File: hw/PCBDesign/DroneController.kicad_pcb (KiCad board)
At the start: 4 copper layers, 100 x 50 mm, 194 parts, among them J1 SerialDebug, J10 SW_B, J11 YTrim, J12 SW_C, J13 TTrim, J14 SW_D, J2 USB_B_Micro, J3 ExtBatt, J4 Conn_ARM_JTAG_SWD_10, J5 EncoderConn, J6 JoystickConn, J7 PTrim, J8 SW_A, J9 RTrim, Q1 MMBT3904, Q2 si2302, Q3 si2302, Q4 si2301, Q5 si2301, SW13 Key_User, SW15 Key_nRESET, SW17 Key_nBOOT, U1 74HC165, U11 74HC595, U13 STM32F446RETx, U14 RN4871, U2 74HC165, U3 74HC165, U4 AT25SF081, U5 AT24C256, U6 NRF24L01_Breakout, U7 BQ24074RGT, U8 AMS1117-3.3, Y1 8MHz Crystal

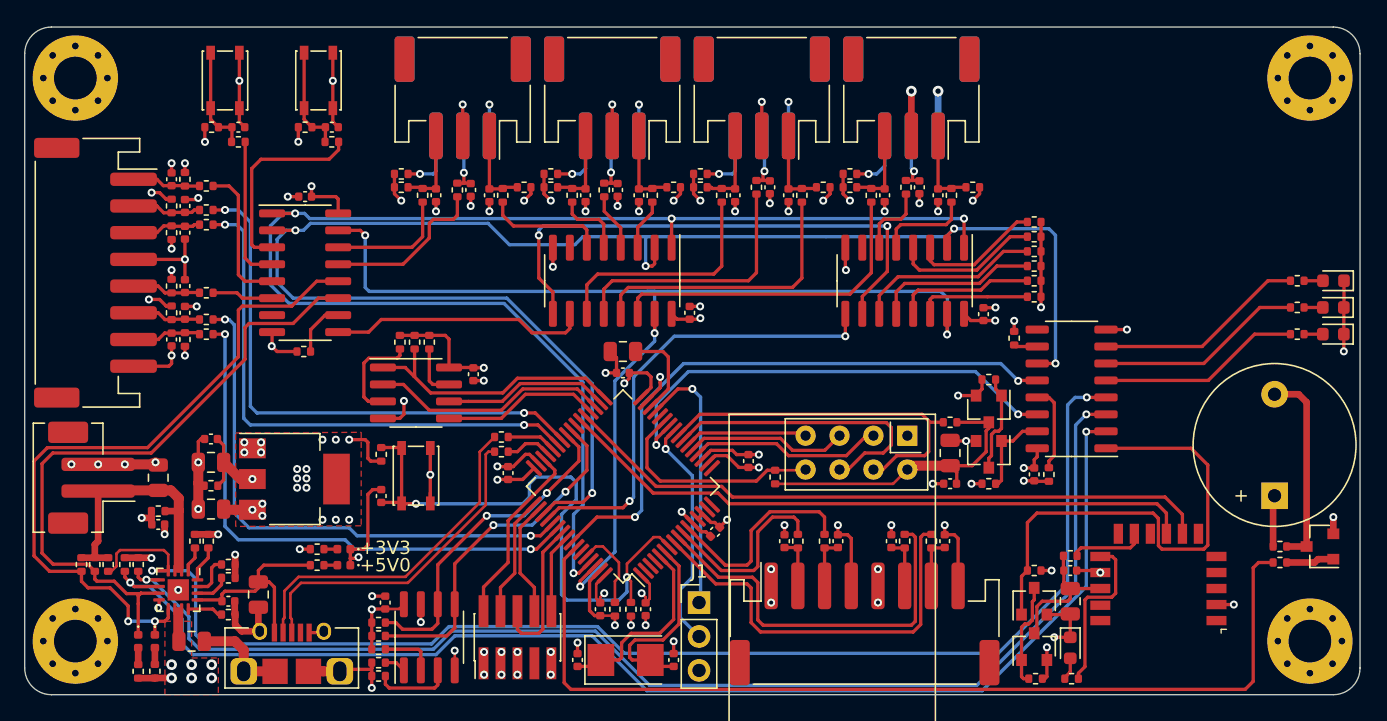
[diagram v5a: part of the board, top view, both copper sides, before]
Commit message: Finished preliminary route of PCB after design review checklist
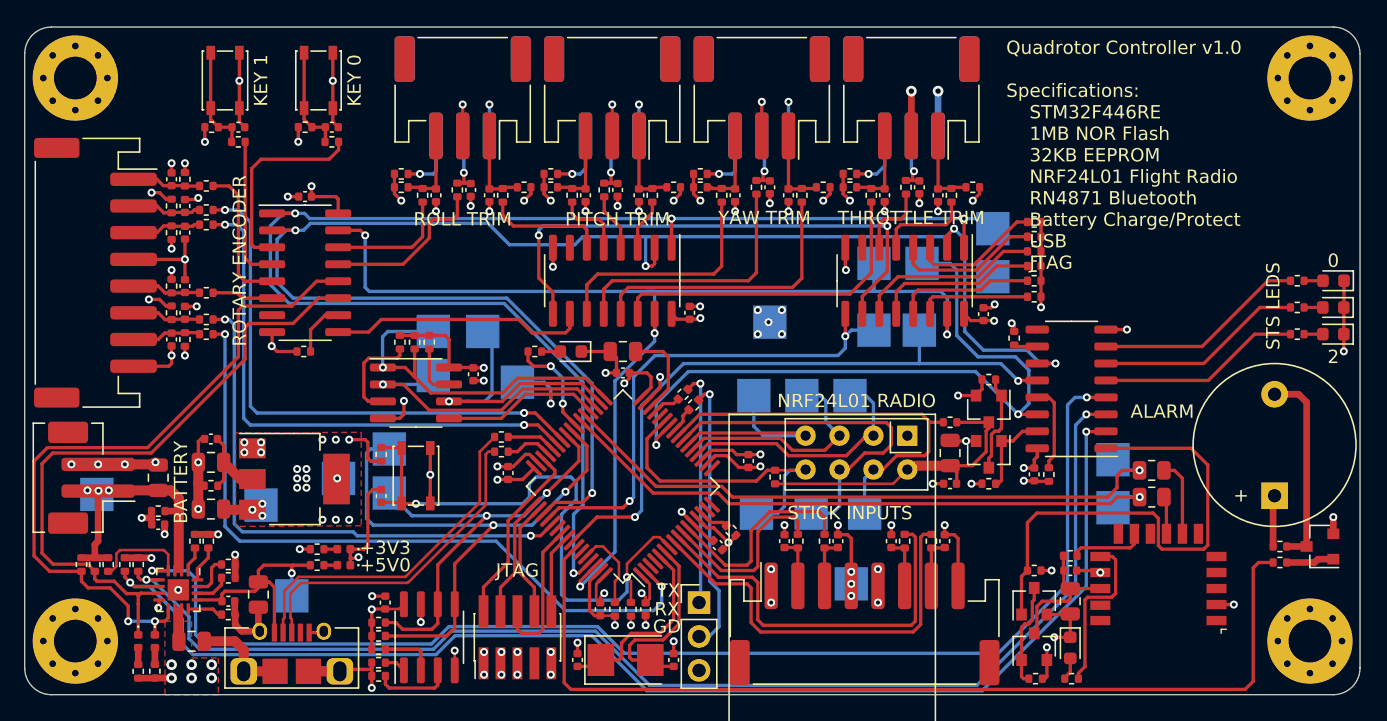
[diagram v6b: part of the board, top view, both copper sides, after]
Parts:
- added D3: STATUS_LED, LED_SMD:LED_0603_1608Metric, F.Cu at (150.9, 104.3)
- added R65: 10k, Resistor_SMD:R_0402_1005Metric, F.Cu at (162.9, 117.7)
- added R86: 0, Resistor_SMD:R_0805_2012Metric, F.Cu at (194.4, 113.2)
- added R87: 0, Resistor_SMD:R_0805_2012Metric, F.Cu at (194.4, 115.2)
- added R89: 10k, Resistor_SMD:R_0402_1005Metric, F.Cu at (160.1, 108.3)
- added R91: 10k, Resistor_SMD:R_0402_1005Metric, F.Cu at (159.3, 107.5)
- added R92: 560, Resistor_SMD:R_0402_1005Metric, F.Cu at (148.2, 104.3)
- added TP1: TestPoint, TestPoint:TestPoint_Pad_2.5x2.5mm, B.Cu at (144.3, 102.8)
- added TP10: TestPoint, TestPoint:TestPoint_Pad_2.5x2.5mm, B.Cu at (164.6, 107.6)
- added TP11: TestPoint, TestPoint:TestPoint_Pad_2.5x2.5mm, B.Cu at (191.5, 116.0)
- added TP12: TestPoint, TestPoint:TestPoint_Pad_2.5x2.5mm, B.Cu at (172.9, 116.4)
- added TP13: TestPoint, TestPoint:TestPoint_Pad_2.5x2.5mm, B.Cu at (171.8, 107.6)
- added TP14: TestPoint, TestPoint:TestPoint_Pad_2.5x2.5mm, B.Cu at (164.8, 116.4)
- added TP15: TestPoint, TestPoint:TestPoint_Pad_2.5x2.5mm, B.Cu at (182.5, 98.7)
- added TP16: TestPoint, TestPoint:TestPoint_Pad_2.5x2.5mm, B.Cu at (177.2, 97.7)
- added TP17: TestPoint, TestPoint:TestPoint_Pad_2.5x2.5mm, B.Cu at (173.6, 102.7)
- added TP18: TestPoint, TestPoint:TestPoint_Pad_2.5x2.5mm, B.Cu at (165.8, 102.1)
- added TP19: TestPoint, TestPoint:TestPoint_Pad_2.5x2.5mm, B.Cu at (177.0, 102.7)
- added TP2: TestPoint, TestPoint:TestPoint_Pad_2.5x2.5mm, B.Cu at (146.9, 106.6)
- added TP20: TestPoint, TestPoint:TestPoint_Pad_2.5x2.5mm, B.Cu at (182.5, 95.1)
- added TP21: TestPoint, TestPoint:TestPoint_Pad_2.5x2.5mm, B.Cu at (173.6, 97.7)
- added TP22: TestPoint, TestPoint:TestPoint_Pad_2.5x2.5mm, B.Cu at (171.9, 121.7)
- added TP23: TestPoint, TestPoint:TestPoint_Pad_2.5x2.5mm, B.Cu at (130.0, 122.6)
- added TP24: TestPoint, TestPoint:TestPoint_Pad_2.5x2.5mm, B.Cu at (115.4, 115.0)
- added TP25: TestPoint, TestPoint:TestPoint_Pad_2.5x2.5mm, B.Cu at (127.7, 115.8)
- added TP26: TestPoint, TestPoint:TestPoint_Pad_2.5x2.5mm, B.Cu at (133.5, 113.8)
- added TP3: TestPoint, TestPoint:TestPoint_Pad_2.5x2.5mm, B.Cu at (137.3, 111.6)
- added TP4: TestPoint, TestPoint:TestPoint_Pad_2.5x2.5mm, B.Cu at (140.6, 106.1)
- added TP5: TestPoint, TestPoint:TestPoint_Pad_2.5x2.5mm, B.Cu at (137.3, 114.9)
- added TP6: TestPoint, TestPoint:TestPoint_Pad_2.5x2.5mm, B.Cu at (140.6, 102.8)
- added TP7: TestPoint, TestPoint:TestPoint_Pad_2.5x2.5mm, B.Cu at (168.2, 107.6)
- added TP8: TestPoint, TestPoint:TestPoint_Pad_2.5x2.5mm, B.Cu at (168.9, 116.4)
- added TP9: TestPoint, TestPoint:TestPoint_Pad_2.5x2.5mm, B.Cu at (191.5, 112.4)
- moved C57 1.02 mm to (161.9, 118.8), turned to 135 degrees
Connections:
- U13 pad 14: +3V3 -> Net-(R65-Pad2)
- U13 pad 2: (no net) -> /Human Machine Interface/ENC0_B
- U13 pad 25: /Processor/DBG_UART_RX -> Net-(R89-Pad1)
- U13 pad 29: /Processor/DBG_UART_TX -> Net-(R91-Pad2)
- U13 pad 39: (no net) -> Net-(R92-Pad2)
- U13 pad 54: /Human Machine Interface/ENC0_B -> (no net)
- U14 pad 7: /Wireless/BT_RX -> Net-(R86-Pad1)
- U14 pad 8: /Wireless/BT_TX -> Net-(R87-Pad1)
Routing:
- net /Processor/KEY_MOSI: track 35.8 -> 53.6 mm
- net /Processor/EEPROM_SDA: track 26.5 -> 42.9 mm
- net /Human Machine Interface/ENC0_B: track 41.5 -> 53.7 mm
- net /Processor/NOR_SCK: track 12.4 -> 20.9 mm, vias 0 -> 1
- net /Processor/EEPROM_SCL: track 24.8 -> 32.8 mm
- net Net-(R92-Pad2): track 0.00 -> 7.82 mm, vias 0 -> 2
- net /Processor/RF24_MISO: track 9.23 -> 15.7 mm
- net /Processor/RF24_nIRQ: track 16.7 -> 23.1 mm
- net /Processor/NOR_nCS: track 20.5 -> 26.8 mm, vias 0 -> 1
- net Net-(R86-Pad1): track 0.00 -> 5.79 mm
- net /Processor/RF24_MOSI: track 22.2 -> 27.3 mm
- net /Processor/RF24_SCK: track 12.1 -> 17.1 mm
- net /Processor/NOR_MOSI: track 11.9 -> 16.4 mm, vias 0 -> 1
- net /Processor/RF24_CE: track 14.5 -> 18.9 mm
- net /Processor/NOR_MISO: track 17.9 -> 22.0 mm, vias 0 -> 1
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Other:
- board text added: "+"
- board text added: "-"
- board text added: "0"
- board text added: "2"
- board text added: "3V3"
- board text added: "5V0"
- board text added: "ALARM"
- board text added: "Analog Ground"
- board text added: "BATT"
- board text added: "BATTERY"
- board text added: "BATT_PROTECT"
- board text added: "Bluetooth"
- board text added: "CE"
- board text added: "CS"
- board text added: "CS_IN"
- board text added: "CS_OUT"
- board text added: "Digital Ground"
- board text added: "Digital IO Shift Registers"
- board text added: "EEPROM"
- board text added: "GD"
- board text added: "IRQ"
- board text added: "JTAG"
- board text added: "KEY 0"
- board text added: "KEY 1"
- board text added: "MISO"
- board text added: "MOSI"
- board text added: "NOR Flash Memory"
- board text added: "NRF24L01 RADIO"
- board text added: "PITCH TRIM"
- board text added: "Piezo Buzzer"
- board text added: "Quadrotor Controller v1.0 Specifications: STM32F446RE 1MB NOR Flash 32KB EEPROM NRF24L01 Flight Radio RN4871 Bluetooth Battery Charge/Protect USB JTAG"
- board text added: "ROLL TRIM"
- board text added: "ROTARY ENCODER"
- board text added: "RX"
- board text added: "SCK"
- board text added: "SCL"
- board text added: "SDA"
- board text added: "STICK INPUTS"
- board text added: "STRB"
- board text added: "STS LEDS"
- board text added: "SWITCH A"
- board text added: "SWITCH B"
- board text added: "SWITCH C"
- board text added: "SWITCH D"
- board text added: "THROTTLE TRIM"
- board text added: "TX"
- board text added: "YAW TRIM"

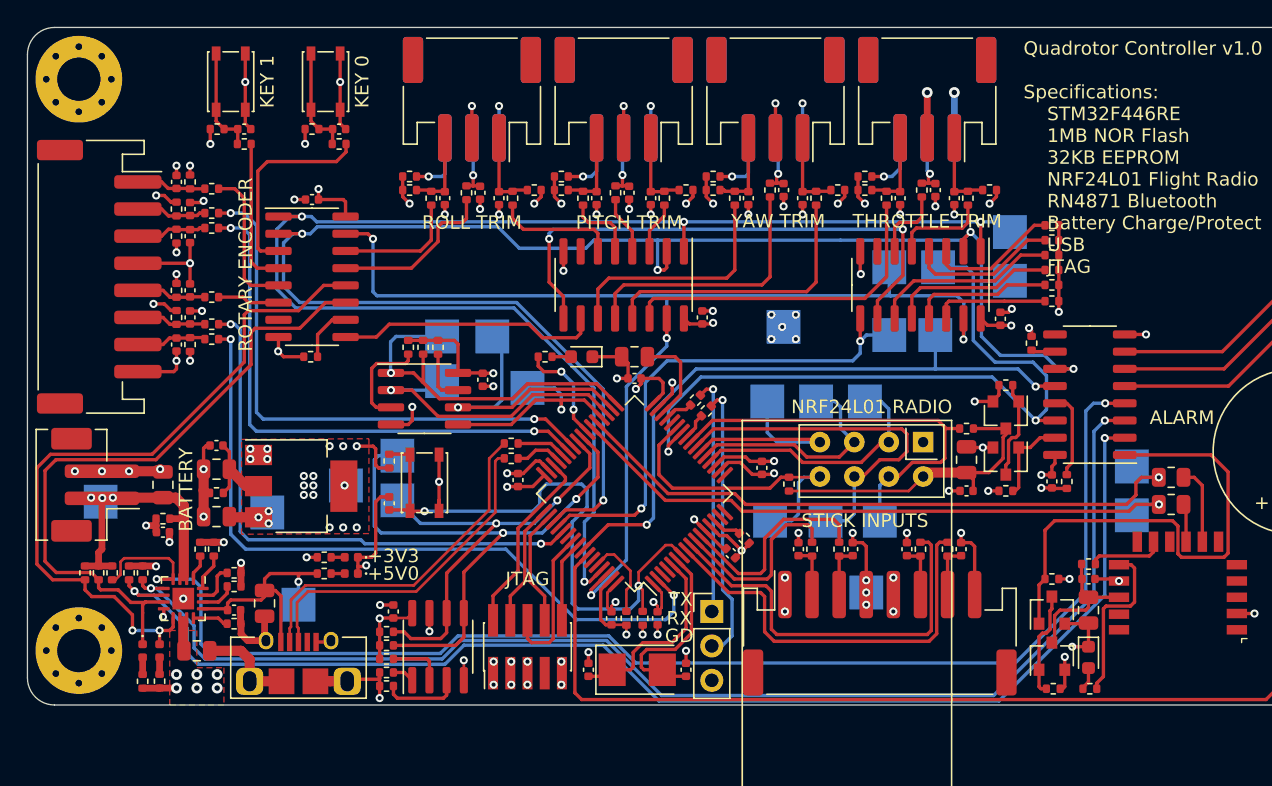
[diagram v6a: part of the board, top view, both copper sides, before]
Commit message: Adjust components for lowest build cost
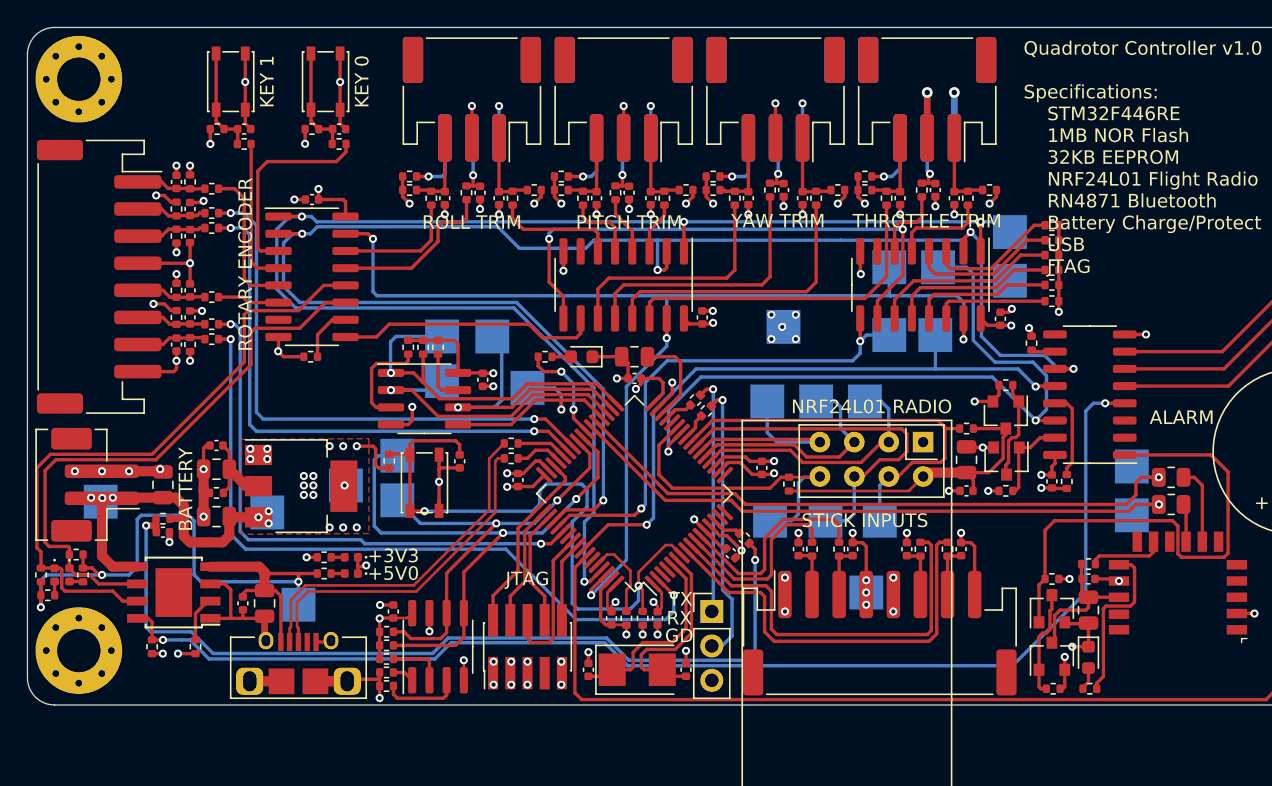
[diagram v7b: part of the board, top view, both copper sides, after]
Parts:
- removed C39: 4.7uF, Capacitor_SMD:C_0805_2012Metric
- removed R72: 4.12k, Resistor_SMD:R_0402_1005Metric
- removed R74, R76: 100k, Resistor_SMD:R_0402_1005Metric
- removed R75: 46.8k, Resistor_SMD:R_0402_1005Metric
- removed R77: 1.18k, Resistor_SMD:R_0402_1005Metric
- removed R78: 1.13k, Resistor_SMD:R_0402_1005Metric
- Q2, Q3: value si2302 -> 2N7002
- Q4, Q5: value si2301 -> LBSS84LT1G
- U7: value BQ24074RGT -> TP4056; footprint Package_DFN_QFN:VQFN-16-1EP_3x3mm_P0.5mm_EP1.6x1.6mm -> PMIC:TP4056_SOP-8-PP
- moved R81 10.4 mm to (111.5, 121.9), turned to 180 degrees
- moved D2 9.56 mm to (112.0, 120.4)
- moved R80 9.00 mm to (114.1, 120.4), turned to 90 degrees
- moved D1 7.78 mm to (113.1, 120.4)
- moved R79 7.21 mm to (122.4, 125.7), turned to 90 degrees
- moved R73 6.20 mm to (119.2, 125.7), turned to 270 degrees
- moved C30 6.05 mm to (141.9, 112.0), turned to 90 degrees
- moved R83 3.25 mm to (111.0, 120.4), turned to 270 degrees
- moved R82 2.13 mm to (113.6, 118.9), turned to 0 degrees
- moved U7 0.83 mm to (120.8, 121.7), turned to 180 degrees
- moved C37 0.82 mm to (125.9, 122.5), turned to 270 degrees
- moved Q2 0.10 mm to (185.6, 122.9)
- moved Q3 0.05 mm to (182.2, 112.0)
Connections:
- C40 pad 1: /Power Supply/V_Batt_Sense -> /Processor/VSense_Batt
- C41 pad 2: /Power Supply/VBattProtectOut -> /Power Supply/vBatt
- R65 pad 1: +3V3 -> /Processor/VSense_Batt
- R73 pad 2: /Power Supply/vBatt -> GND
- R80 pad 2: /Power Supply/VBattProtectOut -> +5V
- R81 pad 2: /Power Supply/VBattProtectOut -> +5V
- R82 pad 2: /Power Supply/vBatt -> +5V
- R83 pad 2: /Power Supply/vBatt -> +5V
- R84 pad 2: /Power Supply/V_Batt_Sense -> /Processor/VSense_Batt
- TP25 pad 1: /Power Supply/VBattProtectOut -> /Power Supply/vBatt
- U11 pad 2: /Processor/BattChgCfg0 -> (no net)
- U11 pad 3: /Processor/BattChgCfg1 -> (no net)
- U7 pad 1: Net-(R79-Pad2) -> GND
- U7 pad 2: /Power Supply/vBatt -> Net-(R79-Pad2)
- U7 pad 3: /Power Supply/vBatt -> GND
- U7 pad 4: /Power Supply/CHG_nEN -> +5V
- U7 pad 5: /Processor/BattChgCfg1 -> /Power Supply/vBatt
- U7 pad 6: /Processor/BattChgCfg0 -> nBatteryPowerGood
- U7 pad 7: nBatteryPowerGood -> nBatteryChargeGood
- U7 pad 8: GND -> /Power Supply/CHG_nEN
- U7 pad 9: nBatteryChargeGood -> (no net)
- U8 pad 3: /Power Supply/VBattProtectOut -> /Power Supply/vBatt
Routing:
- net /Processor/BattChgCfg0: track 96.8 -> 0.00 mm, vias 2 -> 0
- net /Processor/BattChgCfg1: track 94.8 -> 0.00 mm, vias 2 -> 0
- net /Processor/VSense_Batt: track 0.00 -> 64.6 mm, vias 0 -> 2
- net +5V: track 17.8 -> 53.6 mm, vias 1 -> 3
- net /Power Supply/CHG_nEN: track 101.6 -> 91.9 mm
- net GND: track 191.0 -> 182.0 mm, vias 96 -> 93
- net /Power Supply/VBattProtectOut: track 7.71 -> 0.00 mm, vias 9 -> 0
- net nBatteryPowerGood: track 49.0 -> 43.0 mm
- net nBatteryChargeGood: track 52.5 -> 46.8 mm, vias 2 -> 0
- net /Human Machine Interface/nRESET: track 44.5 -> 48.5 mm
- net /Power Supply/vBatt: track 20.5 -> 24.1 mm, vias 3 -> 6
- net Net-(R72-Pad1): track 3.14 -> 0.00 mm
- net Net-(R78-Pad1): track 2.73 -> 0.00 mm
- net Net-(R77-Pad1): track 2.66 -> 0.00 mm
- net Net-(R75-Pad2): track 2.58 -> 0.00 mm
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- added copper zone on In2.Cu, net /Power Supply/vBatt
- removed copper zone on F.Cu, net /Power Supply/VBattProtectOut
- removed copper zone on In2.Cu, net /Power Supply/VBattProtectOut
